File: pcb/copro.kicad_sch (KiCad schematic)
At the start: 5 parts, among them U39 74HC02, U40 ATmega1284-P, U41 74HC245, U42 74HC245, U43 74HC245

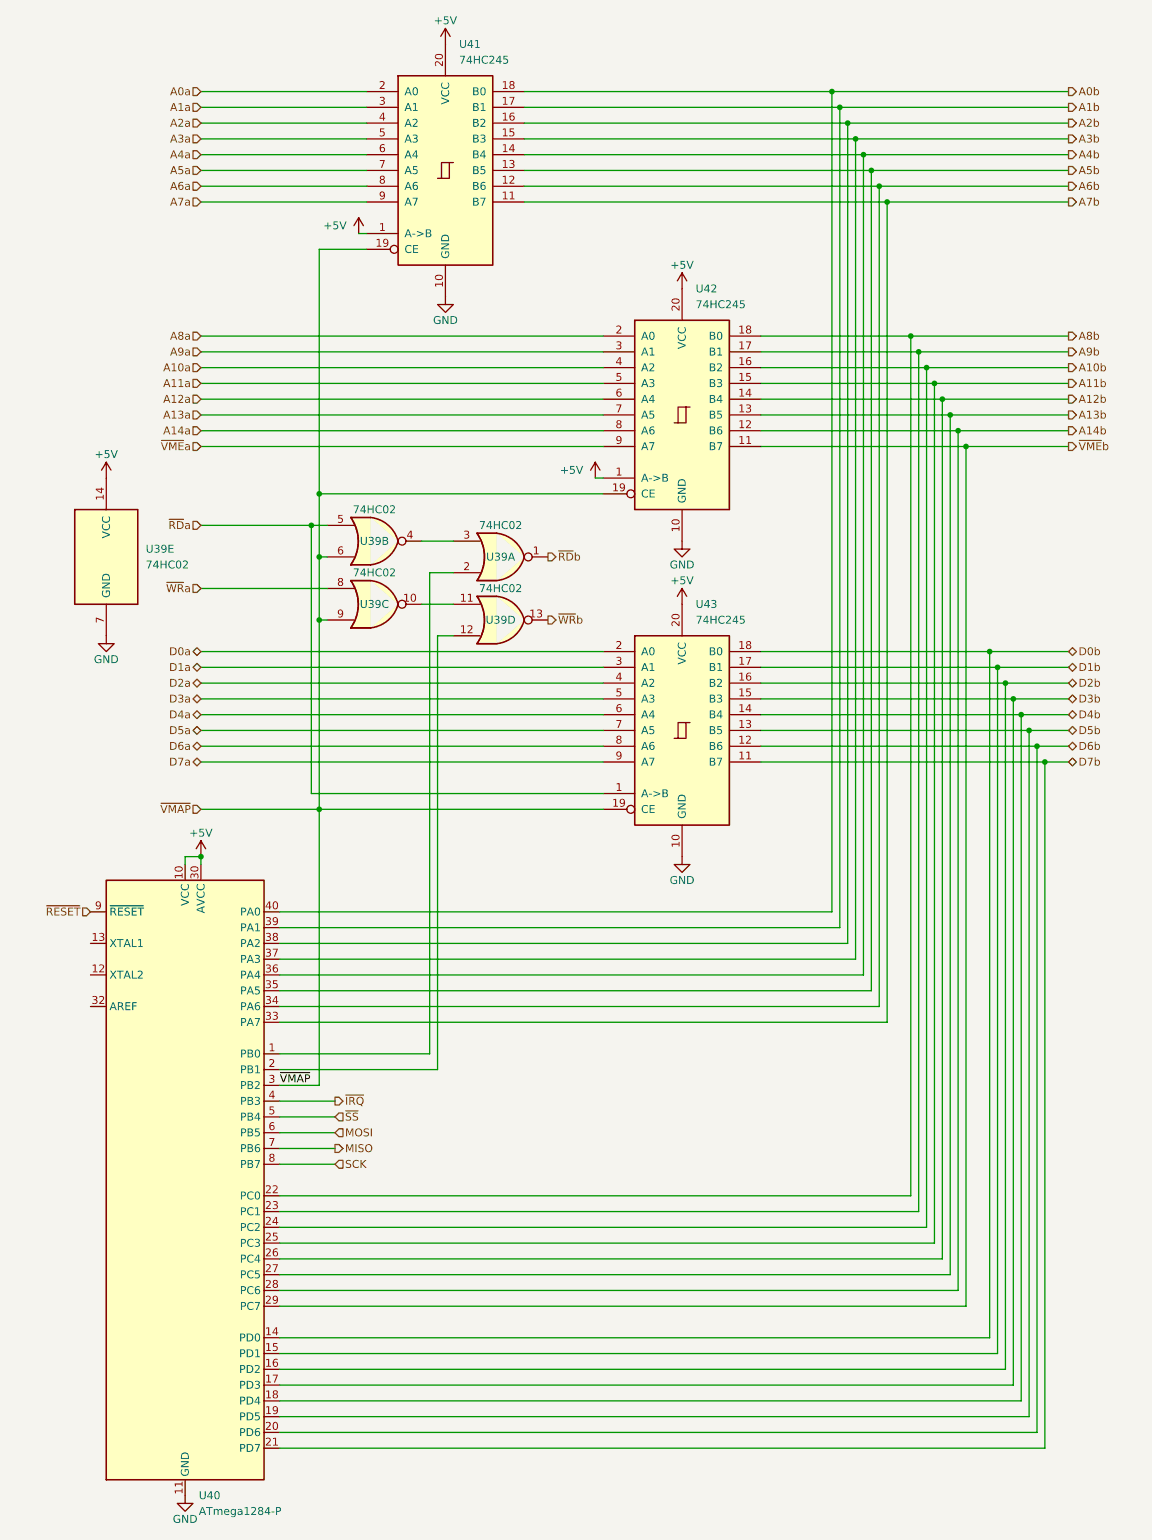
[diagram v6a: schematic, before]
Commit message: WIP PCB (add bypass caps, minor fixes)
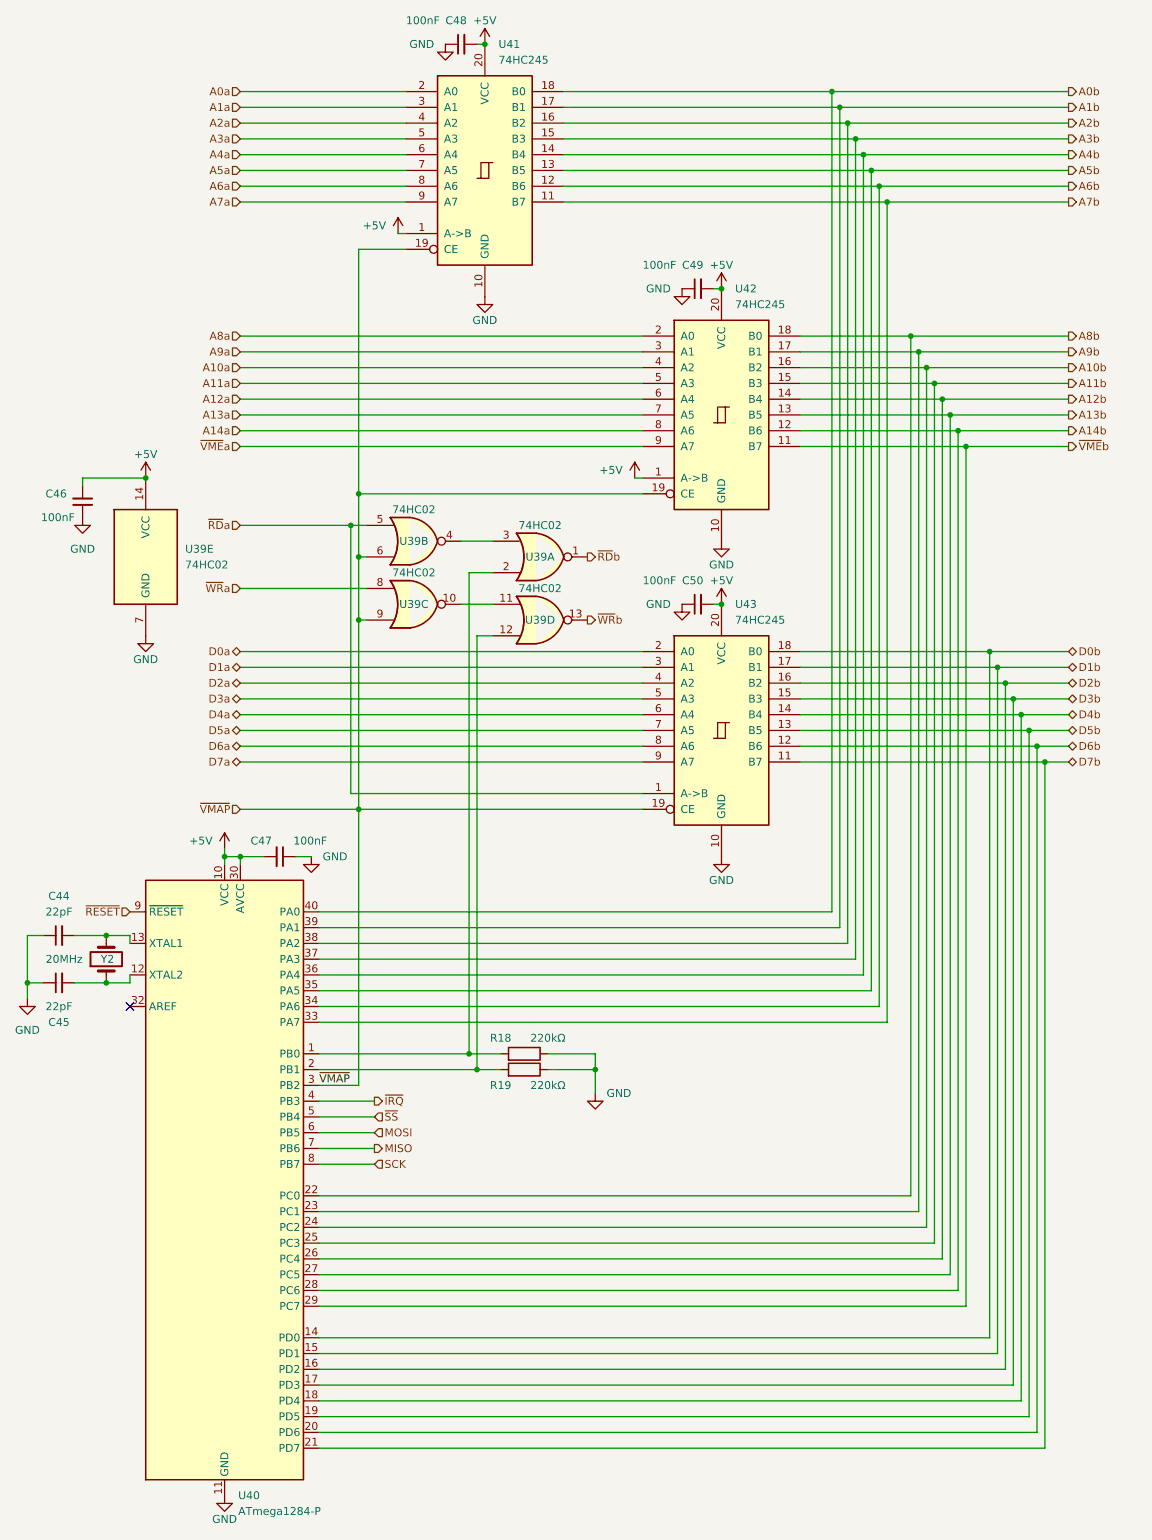
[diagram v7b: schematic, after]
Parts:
- added C44, C45: 22pF, symbol Device:C_Small
- added C46, C47, C48, C49, C50: 100nF, symbol Device:C_Small
- added R18, R19: 220kΩ, symbol Device:R
- added Y2: 20MHz, symbol Device:Crystal
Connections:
- net +5V: now also C46.2, C47.2, C48.2, C49.2, C50.2
- net GND: now also C44.1, C45.1, C46.1, C47.1, C48.1, C49.1, C50.1, R18.1, R19.1
- net at U39.12, U40.2 (PB1): now also R19.2
- net at U39.2, U40.1 (PB0): now also R18.2
- net at U40.12 (XTAL2): now also C45.2, Y2.1
- net at U40.13 (XTAL1): now also C44.2, Y2.2
- no-connect marks 0 -> 1
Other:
- moved on the sheet: U39A, U39B, U39C, U39D, U39E, U40, U41, U42, U43
